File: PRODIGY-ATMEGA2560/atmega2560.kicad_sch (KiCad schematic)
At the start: 2 parts, among them U1 ATmega2560-16A, Y1 Crystal

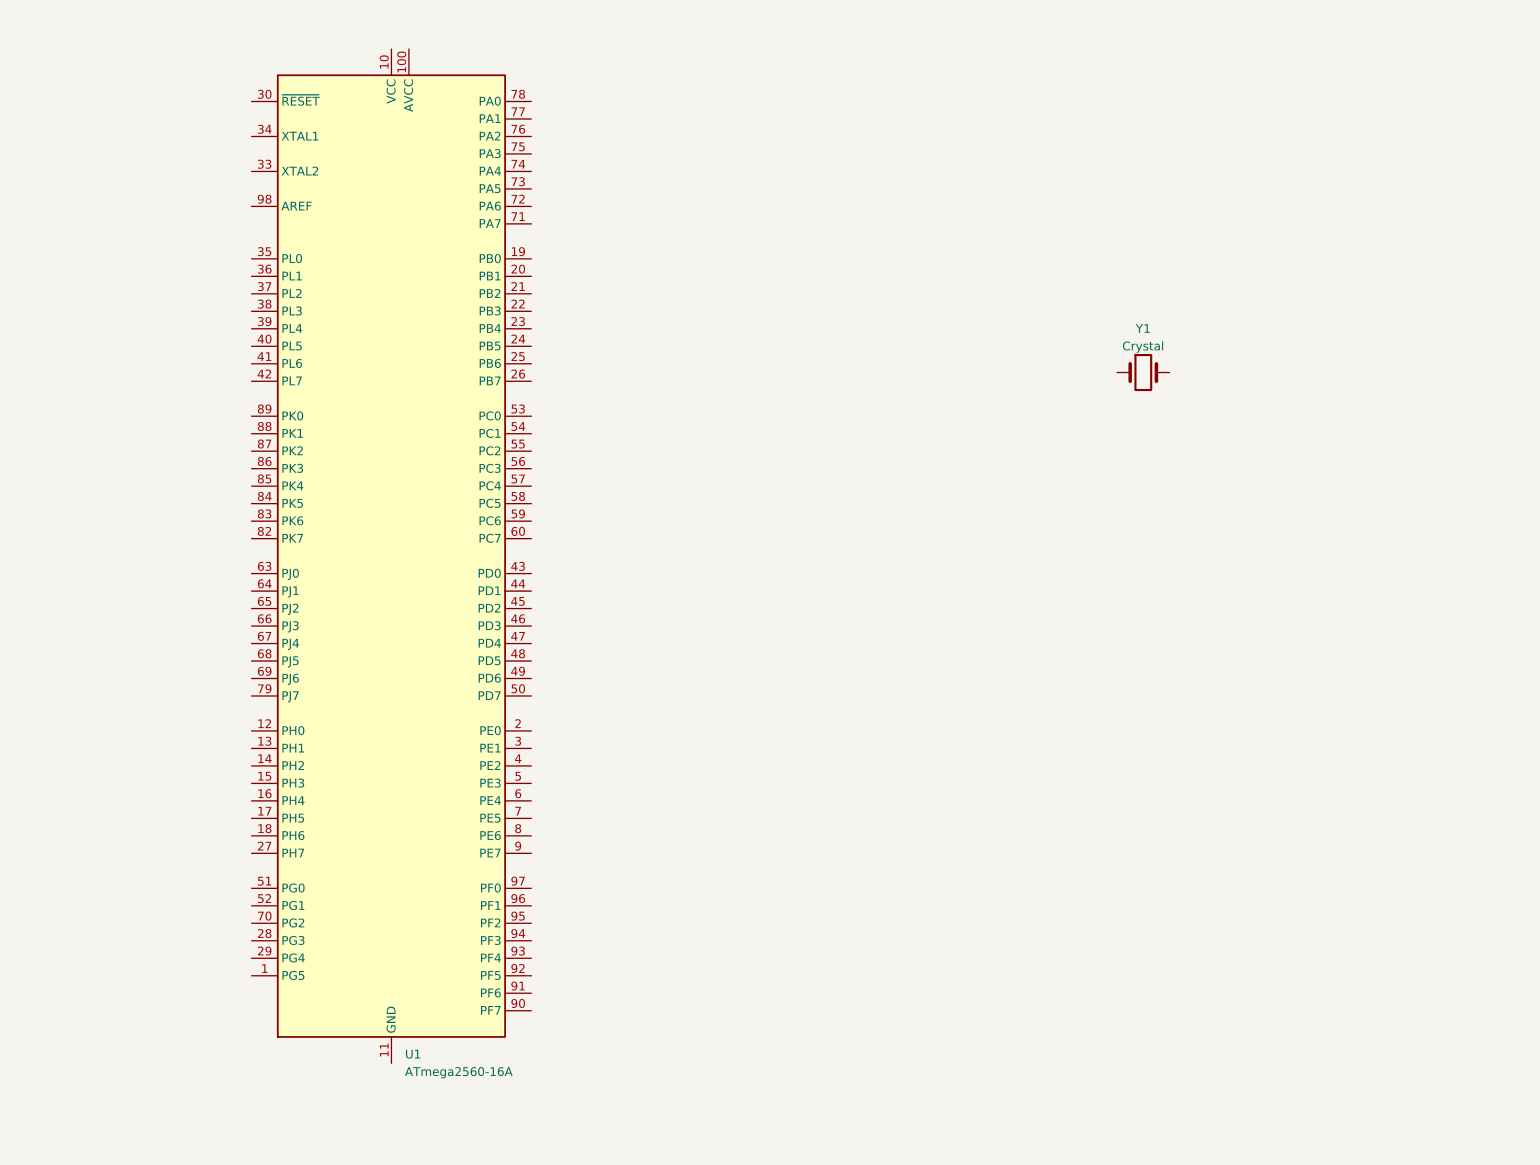
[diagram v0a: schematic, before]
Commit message: ATMEGA2560 schematic finished
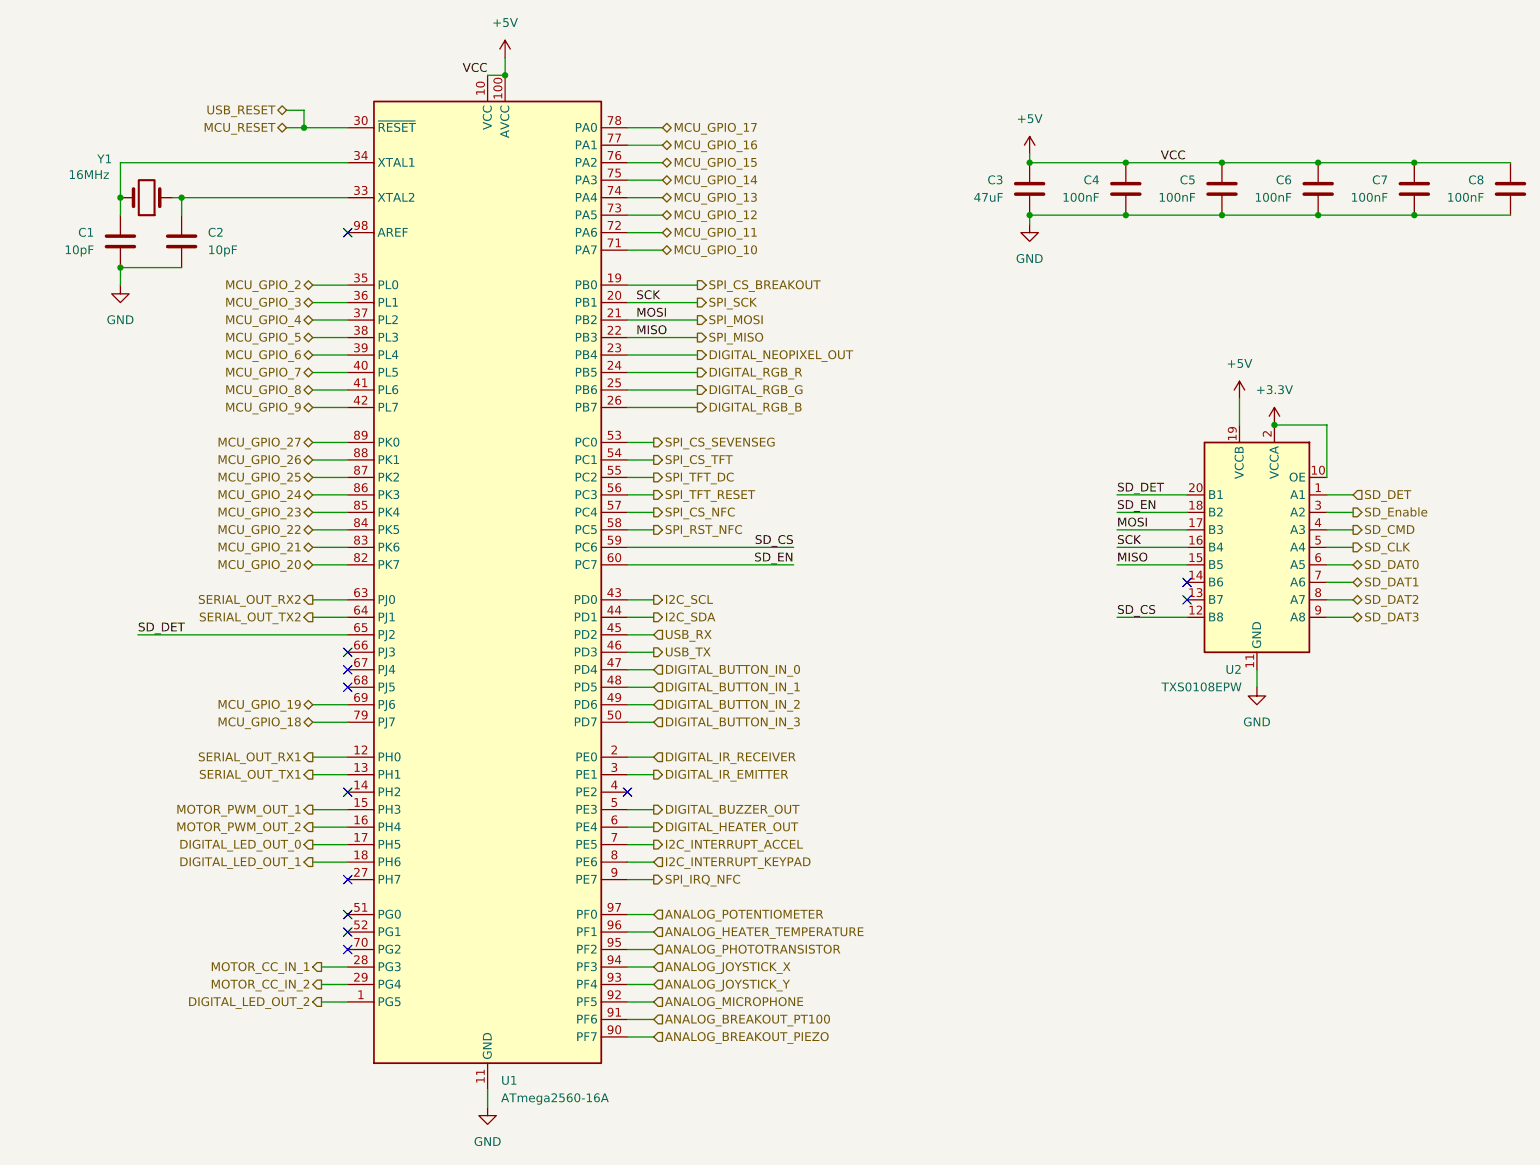
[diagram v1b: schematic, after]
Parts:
- added C1, C2: 10pF, symbol Device:C
- added C3: 47uF, symbol Device:C
- added C4, C5, C6, C7, C8: 100nF, symbol Device:C
- added U2: TXS0108EPW, Package_SO:TSSOP-20_4.4x6.5mm_P0.65mm, symbol Logic_LevelTranslator:TXS0108EPW
- Y1: value Crystal -> 16MHz
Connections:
- net at Y1.1: now also U1.33 (XTAL2), C2.1
- net at Y1.2: now also U1.34 (XTAL1), C1.1
- net DIGITAL_LED_OUT_2: now reaches U1.1 (PG5)
- net +5V: now reaches U1.10 (VCC), U1.31 (VCC), U1.61 (VCC), U1.80 (VCC)
- net +5V: now also U1.100 (AVCC), C3.1, C4.1, C5.1, C6.1, C7.1, C8.1, U2.19 (VCCB)
- net GND: now reaches U1.11 (GND), U1.32 (GND), U1.62 (GND), U1.81 (GND), U1.99 (GND)
- net GND: now also C1.2, C2.2, C3.2, C4.2, C5.2, C6.2, C7.2, C8.2, U2.11 (GND)
- net SERIAL_OUT_RX1: now reaches U1.12 (PH0)
- net SERIAL_OUT_TX1: now reaches U1.13 (PH1)
- net MOTOR_PWM_OUT_1: now reaches U1.15 (PH3)
- net MOTOR_PWM_OUT_2: now reaches U1.16 (PH4)
- net DIGITAL_LED_OUT_0: now reaches U1.17 (PH5)
- net DIGITAL_LED_OUT_1: now reaches U1.18 (PH6)
- net SPI_CS_BREAKOUT: now reaches U1.19 (PB0)
- net DIGITAL_IR_RECEIVER: now reaches U1.2 (PE0)
- net SPI_SCK: now reaches U1.20 (PB1)
- net SPI_SCK: now also U2.16 (B4)
- net SPI_MOSI: now reaches U1.21 (PB2)
- net SPI_MOSI: now also U2.17 (B3)
- net SPI_MISO: now reaches U1.22 (PB3)
- net SPI_MISO: now also U2.15 (B5)
- net DIGITAL_NEOPIXEL_OUT: now reaches U1.23 (PB4)
- net DIGITAL_RGB_R: now reaches U1.24 (PB5)
- net DIGITAL_RGB_G: now reaches U1.25 (PB6)
- net DIGITAL_RGB_B: now reaches U1.26 (PB7)
- net MOTOR_CC_IN_1: now reaches U1.28 (PG3)
- net MOTOR_CC_IN_2: now reaches U1.29 (PG4)
- net DIGITAL_IR_EMITTER: now reaches U1.3 (PE1)
- net MCU_RESET: now reaches U1.30 (~{RESET})
- net MCU_GPIO_2: now reaches U1.35 (PL0)
- net MCU_GPIO_3: now reaches U1.36 (PL1)
- net MCU_GPIO_4: now reaches U1.37 (PL2)
- net MCU_GPIO_5: now reaches U1.38 (PL3)
- net MCU_GPIO_6: now reaches U1.39 (PL4)
- net MCU_GPIO_7: now reaches U1.40 (PL5)
- net MCU_GPIO_8: now reaches U1.41 (PL6)
- net MCU_GPIO_9: now reaches U1.42 (PL7)
- net I2C_SCL: now reaches U1.43 (PD0)
- net I2C_SDA: now reaches U1.44 (PD1)
- net USB_RX: now reaches U1.45 (PD2)
- net USB_TX: now reaches U1.46 (PD3)
- net DIGITAL_BUTTON_IN_0: now reaches U1.47 (PD4)
- net DIGITAL_BUTTON_IN_1: now reaches U1.48 (PD5)
- net DIGITAL_BUTTON_IN_2: now reaches U1.49 (PD6)
- net DIGITAL_BUZZER_OUT: now reaches U1.5 (PE3)
- net DIGITAL_BUTTON_IN_3: now reaches U1.50 (PD7)
- net SPI_CS_SEVENSEG: now reaches U1.53 (PC0)
- net SPI_CS_TFT: now reaches U1.54 (PC1)
- net SPI_TFT_DC: now reaches U1.55 (PC2)
- net SPI_TFT_RESET: now reaches U1.56 (PC3)
- net SPI_CS_NFC: now reaches U1.57 (PC4)
- net SPI_RST_NFC: now reaches U1.58 (PC5)
- net SD_CS: now reaches U1.59 (PC6)
- net SD_CS: now also U2.12 (B8)
- net DIGITAL_HEATER_OUT: now reaches U1.6 (PE4)
- net SD_EN: now reaches U1.60 (PC7)
- net SD_EN: now also U2.18 (B2)
- net SERIAL_OUT_RX2: now reaches U1.63 (PJ0)
- net SERIAL_OUT_TX2: now reaches U1.64 (PJ1)
- net SD_DET: now reaches U1.65 (PJ2)
- net SD_DET: now also U2.1 (A1), U2.20 (B1)
- net MCU_GPIO_19: now reaches U1.69 (PJ6)
- net I2C_INTERRUPT_ACCEL: now reaches U1.7 (PE5)
- net MCU_GPIO_10: now reaches U1.71 (PA7)
- net MCU_GPIO_11: now reaches U1.72 (PA6)
- net MCU_GPIO_12: now reaches U1.73 (PA5)
- net MCU_GPIO_13: now reaches U1.74 (PA4)
- net MCU_GPIO_14: now reaches U1.75 (PA3)
- net MCU_GPIO_15: now reaches U1.76 (PA2)
- net MCU_GPIO_16: now reaches U1.77 (PA1)
- net MCU_GPIO_17: now reaches U1.78 (PA0)
- net MCU_GPIO_18: now reaches U1.79 (PJ7)
- net I2C_INTERRUPT_KEYPAD: now reaches U1.8 (PE6)
- net MCU_GPIO_20: now reaches U1.82 (PK7)
- net MCU_GPIO_21: now reaches U1.83 (PK6)
- net MCU_GPIO_22: now reaches U1.84 (PK5)
- net MCU_GPIO_23: now reaches U1.85 (PK4)
- net MCU_GPIO_24: now reaches U1.86 (PK3)
- net MCU_GPIO_25: now reaches U1.87 (PK2)
- net MCU_GPIO_26: now reaches U1.88 (PK1)
- net MCU_GPIO_27: now reaches U1.89 (PK0)
- net SPI_IRQ_NFC: now reaches U1.9 (PE7)
- net ANALOG_BREAKOUT_PIEZO: now reaches U1.90 (PF7)
- net ANALOG_BREAKOUT_PT100: now reaches U1.91 (PF6)
- net ANALOG_MICROPHONE: now reaches U1.92 (PF5)
- net ANALOG_JOYSTICK_Y: now reaches U1.93 (PF4)
- net ANALOG_JOYSTICK_X: now reaches U1.94 (PF3)
- net ANALOG_PHOTOTRANSISTOR: now reaches U1.95 (PF2)
- net ANALOG_HEATER_TEMPERATURE: now reaches U1.96 (PF1)
- net ANALOG_POTENTIOMETER: now reaches U1.97 (PF0)
- new net +3.3V: U2.10 (OE), U2.2 (VCCA)
- new net SD_CLK: U2.5 (A4)
- new net SD_CMD: U2.4 (A3)
- new net SD_DAT0: U2.6 (A5)
- new net SD_DAT1: U2.7 (A6)
- new net SD_DAT2: U2.8 (A7)
- new net SD_DAT3: U2.9 (A8)
- new net SD_Enable: U2.3 (A2)
- no-connect marks 0 -> 12
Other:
- moved on the sheet: U1, Y1

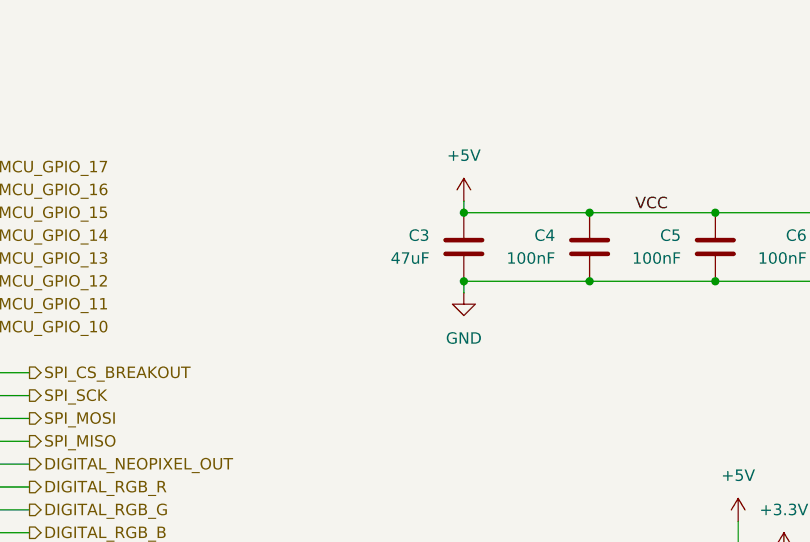
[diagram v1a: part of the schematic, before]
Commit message: All footprint assosiations have been made across all schematics.
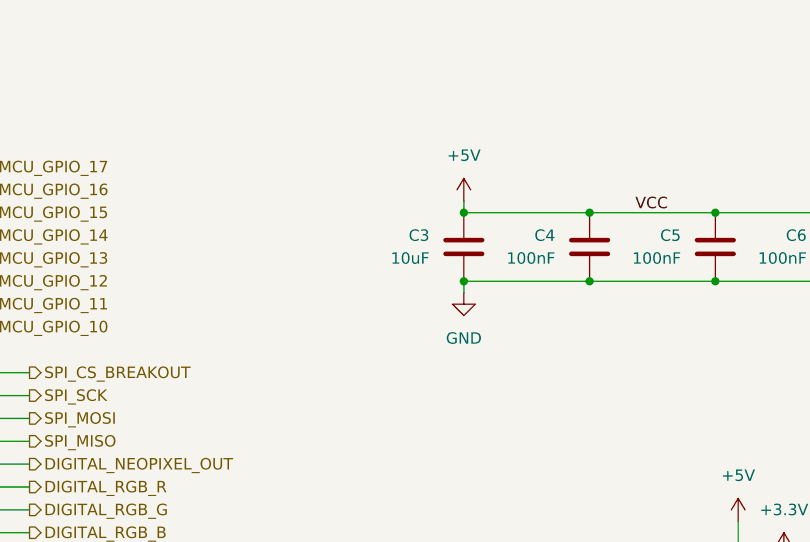
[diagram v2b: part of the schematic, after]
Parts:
- C1, C2, C4, C5, C6, C7, C8: footprint (none) -> Capacitor_SMD:C_0603_1608Metric
- C3: value 47uF -> 10uF; footprint (none) -> Capacitor_SMD:C_0805_2012Metric
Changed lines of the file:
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@@
 	)
 	(junction
-		(at 193.04 50.8)
-		(diameter 0)
-		(color 0 0 0 0)
-	)
-	(junction
 		(at 234.95 50.8)
 		(diameter 0)
@@
 	)
 	(junction
+		(at 193.04 50.8)
+		(diameter 0)
+		(color 0 0 0 0)
+	)
+	(junction
 		(at 207.01 50.8)
 		(diameter 0)
@@
 			)
 		)
-		(property "Footprint" ""
+		(property "Footprint" "Capacitor_SMD:C_0603_1608Metric"
 			(at 70.8152 58.42 0)
 			(effects
@@
 	)
 	(symbol
+		(lib_id "Device:C")
+		(at 193.04 46.99 0)
+		(mirror y)
+		(unit 1)
+		(exclude_from_sim no)
+		(in_bom yes)
+		(on_board yes)
+		(dnp no)
+		(property "Reference" "C3"
+			(at 189.23 45.7199 0)
+			(effects
+				(font
+					(size 1.27 1.27)
+				)
+				(justify left)
+			)
+		)
+		(property "Value" "10uF"
+			(at 189.23 48.2599 0)
+			(effects
+				(font
+					(size 1.27 1.27)
+				)
+				(justify left)
+			)
+		)
+		(property "Footprint" "Capacitor_SMD:C_0805_2012Metric"
+			(at 192.0748 50.8 0)
+			(effects
+				(font
+					(size 1.27 1.27)
+				)
+				(hide yes)
+			)
+		)
+		(property "Datasheet" "~"
+			(at 193.04 46.99 0)
+			(effects
+				(font
+					(size 1.27 1.27)
+				)
+				(hide yes)
+			)
+		)
+		(property "Description" "Unpolarized capacitor"
+			(at 193.04 46.99 0)
+			(effects
+				(font
+					(size 1.27 1.27)
+				)
+				(hide yes)
+			)
+		)
+		(pin "2"
+		)
+		(pin "1"
+		)
+		(instances
+			(project "PRODIGY-ATMEGA2560"
+				(path "/58f705c8-87df-406b-b9b9-efbb33b15a7f/4822de75-534b-4878-b140-638cea37e7de"
+					(reference "C3")
+					(unit 1)
+				)
+			)
+		)
+	)
+	(symbol
 		(lib_id "Logic_LevelTranslator:TXS0108EPW")
 		(at 226.06 99.06 0)
@@
 			)
 		)
-		(property "Footprint" ""
+		(property "Footprint" "Capacitor_SMD:C_0603_1608Metric"
 			(at 261.9248 50.8 0)
 			(effects
@@
 			)
 		)
-		(property "Footprint" ""
+		(property "Footprint" "Capacitor_SMD:C_0603_1608Metric"
 			(at 220.0148 50.8 0)
 			(effects
@@
 			)
 		)
-		(property "Footprint" ""
+		(property "Footprint" "Capacitor_SMD:C_0603_1608Metric"
 			(at 59.9948 58.42 0)
 			(effects
@@
 	(symbol
 		(lib_id "Device:C")
-		(at 193.04 46.99 0)
-		(mirror y)
-		(unit 1)
-		(exclude_from_sim no)
-		(in_bom yes)
-		(on_board yes)
-		(dnp no)
-		(property "Reference" "C3"
-			(at 189.23 45.7199 0)
-			(effects
-				(font
-					(size 1.27 1.27)
-				)
-				(justify left)
-			)
-		)
-		(property "Value" "47uF"
-			(at 189.23 48.2599 0)
-			(effects
-				(font
-					(size 1.27 1.27)
-				)
-				(justify left)
-			)
-		)
-		(property "Footprint" ""
-			(at 192.0748 50.8 0)
-			(effects
-				(font
-					(size 1.27 1.27)
-				)
-				(hide yes)
-			)
-		)
-		(property "Datasheet" "~"
-			(at 193.04 46.99 0)
-			(effects
-				(font
-					(size 1.27 1.27)
-				)
-				(hide yes)
-			)
-		)
-		(property "Description" "Unpolarized capacitor"
-			(at 193.04 46.99 0)
-			(effects
-				(font
-					(size 1.27 1.27)
-				)
-				(hide yes)
-			)
-		)
-		(pin "2"
-		)
-		(pin "1"
-		)
-		(instances
-			(project "PRODIGY-ATMEGA2560"
-				(path "/58f705c8-87df-406b-b9b9-efbb33b15a7f/4822de75-534b-4878-b140-638cea37e7de"
-					(reference "C3")
-					(unit 1)
-				)
-			)
-		)
-	)
-	(symbol
-		(lib_id "Device:C")
 		(at 234.95 46.99 0)
 		(mirror y)
@@
 			)
 		)
-		(property "Footprint" ""
+		(property "Footprint" "Capacitor_SMD:C_0603_1608Metric"
 			(at 233.9848 50.8 0)
 			(effects
@@
 			)
 		)
-		(property "Footprint" ""
+		(property "Footprint" "Capacitor_SMD:C_0603_1608Metric"
 			(at 247.9548 50.8 0)
 			(effects
@@
 			)
 		)
-		(property "Footprint" ""
+		(property "Footprint" "Capacitor_SMD:C_0603_1608Metric"
 			(at 206.0448 50.8 0)
 			(effects
